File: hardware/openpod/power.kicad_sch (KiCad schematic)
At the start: 21 parts

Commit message: update power and audio
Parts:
- removed C51: 10uF, symbol Device:C
- removed LDO2: MIC5504-3.3YM5, Package_TO_SOT_SMD:SOT-23-5, symbol Regulator_Linear:MIC5504-3.3YM5
- added AP7312: ~, Package_TO_SOT_SMD:SOT-23-6, symbol openpod:AP7312
- added FB1, FB2: FerriteBead, symbol Device:FerriteBead
- C52: value 10uF -> 1uF
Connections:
- net GND: now also AP7312.2 (GND), FB2.1
- net 3.3-audio renamed +1V8
- net +1V8: now also AP7312.6 (OUT1)
- net 3.3V: no longer names the net of Buck-converter2.3 (EN), Buck-converter2.4 (FB), C50.1, L2.2
- net 3.3V: now also FB1.1
- new net +3.3V: AP7312.3 (EN2), AP7312.4 (EN1), AP7312.5 (IN), FB1.2
- new net +3.3VA: AP7312.1 (OUT2)
- new net GNDA: FB2.2

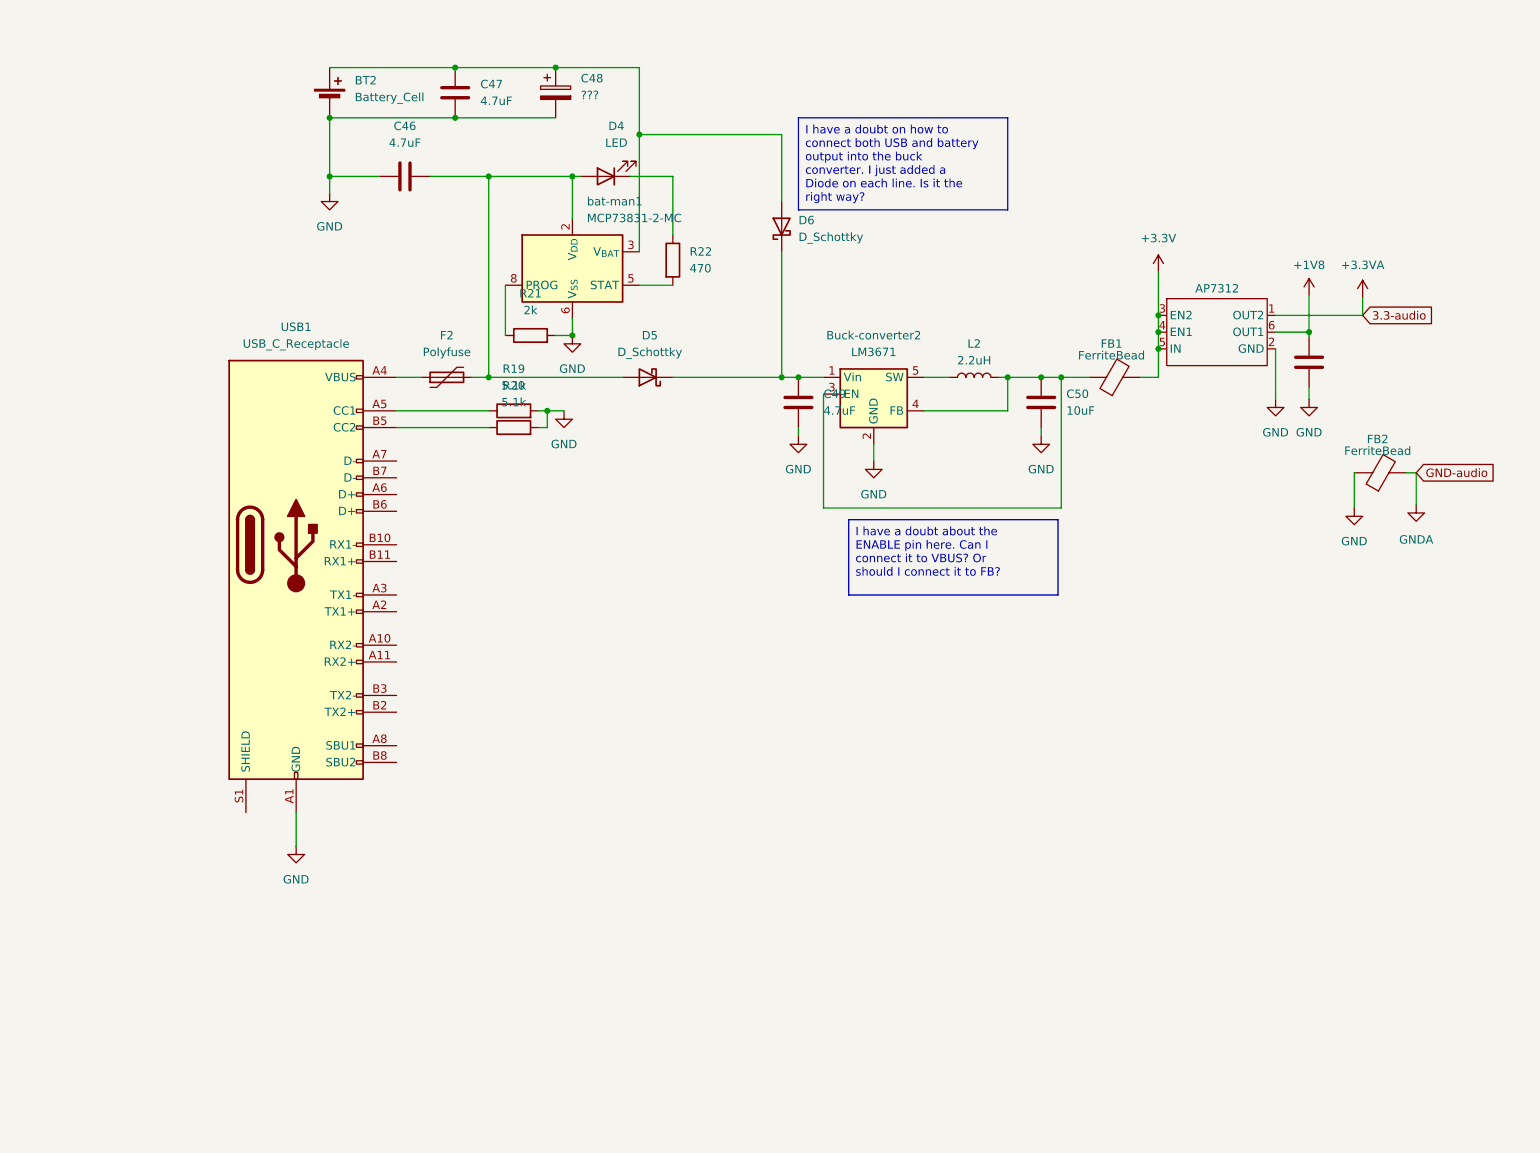
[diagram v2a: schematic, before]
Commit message: added UART converter
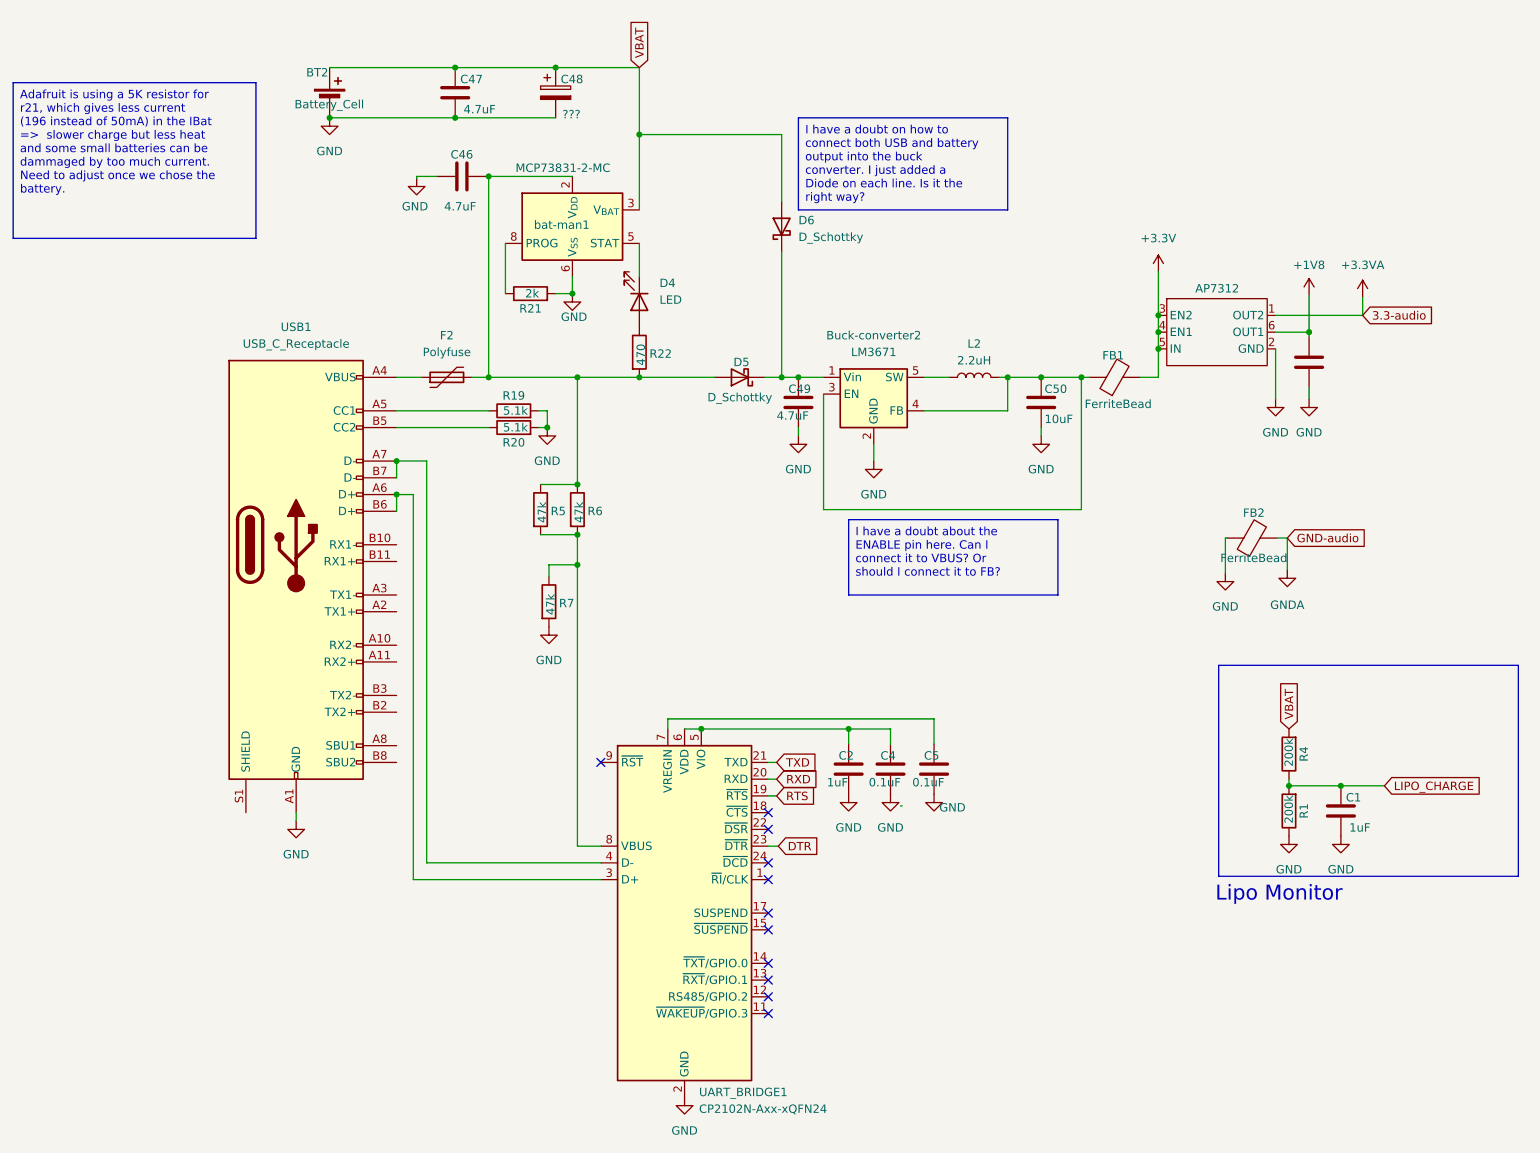
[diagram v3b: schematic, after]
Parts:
- added C1, C2: 1uF, symbol Device:C
- added C4, C5: 0.1uF, symbol Device:C
- added R1, R4: 200k, symbol Device:R
- added R5, R6, R7: 47k, symbol Device:R
- added UART_BRIDGE1: CP2102N-Axx-xQFN24, Package_DFN_QFN:QFN-24-1EP_4x4mm_P0.5mm_EP2.6x2.6mm, symbol Interface_USB:CP2102N-Axx-xQFN24
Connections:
- net GND: now also C1.2, C2.2, C4.2, C5.2, R1.1, R7.2, UART_BRIDGE1.2 (GND), UART_BRIDGE1.25 (GND)
- net at D4.1 (K): now also bat-man1.5 (STAT); no longer R22.1
- net at C46.2, D5.2 (A), F2.2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: now also R22.2, R5.1, R6.1; no longer D4.2 (A)
- net VBAT: now reaches BT2.1 (+), C47.1, C48.1, D6.2 (A), bat-man1.3 (V_{BAT}), bat-man1.4 (V_{BAT})
- net VBAT: now also R4.2
- net at USB1.A6 (D+): now also USB1.B6 (D+), UART_BRIDGE1.3 (D+)
- net at USB1.A7 (D-): now also USB1.B7 (D-), UART_BRIDGE1.4 (D-)
- new net: D4.2 (A), R22.1
- new net: C2.1, C4.1, UART_BRIDGE1.5 (VIO), UART_BRIDGE1.6 (VDD)
- new net: C5.1, UART_BRIDGE1.7 (VREGIN)
- new net: R5.2, R6.2, R7.1, UART_BRIDGE1.8 (VBUS)
- new net DTR: UART_BRIDGE1.23 (~{DTR})
- new net LIPO_CHARGE: C1.1, R1.2, R4.1
- new net RTS: UART_BRIDGE1.19 (~{RTS})
- new net RXD: UART_BRIDGE1.20 (RXD)
- new net TXD: UART_BRIDGE1.21 (TXD)
- no-connect marks 0 -> 11
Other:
- note added: "Lipo Monitor"
- moved on the sheet: C46, D4, D5, FB2, R21, R22, bat-man1

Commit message: added bluetooth
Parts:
- BT2: value Battery_Cell -> 900mah; Part number (none) -> LP053450
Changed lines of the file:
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@@
     (stroke (width 0) (type default))
   )
-  (wire (pts (xy 80.772 151.892) (xy 80.772 90.932))
+  (wire (pts (xy 95.25 151.892) (xy 95.25 90.932))
     (stroke (width 0) (type default))
   )
@@
     (stroke (width 0) (type default))
   )
-  (wire (pts (xy 78.74 154.432) (xy 107.188 154.432))
+  (wire (pts (xy 92.71 154.432) (xy 107.188 154.432))
     (stroke (width 0) (type default))
   )
@@
     (stroke (width 0) (type default))
   )
-  (wire (pts (xy 78.74 96.012) (xy 78.74 154.432))
+  (wire (pts (xy 92.71 96.012) (xy 92.71 154.432))
     (stroke (width 0) (type default))
   )
@@
     (stroke (width 0) (type default))
   )
-  (wire (pts (xy 76.2 96.012) (xy 78.74 96.012))
+  (wire (pts (xy 76.2 96.012) (xy 92.71 96.012))
     (stroke (width 0) (type default))
   )
@@
     (stroke (width 0) (type default))
   )
-  (wire (pts (xy 76.2 90.932) (xy 80.772 90.932))
-    (stroke (width 0) (type default))
-  )
-  (wire (pts (xy 107.188 151.892) (xy 80.772 151.892))
+  (wire (pts (xy 76.2 90.932) (xy 95.25 90.932))
+    (stroke (width 0) (type default))
+  )
+  (wire (pts (xy 107.188 151.892) (xy 95.25 151.892))
     (stroke (width 0) (type default))
   )
@@
       (effects (font (size 1.27 1.27)) (justify left))
     )
-    (property "Value" "Battery_Cell" (at 60.706 36.83 0)
+    (property "Value" "900mah" (at 60.706 36.83 0)
       (effects (font (size 1.27 1.27)) (justify left))
     )
@@
       (effects (font (size 1.27 1.27)) hide)
     )
-    (property "Datasheet" "~" (at 66.04 34.798 90)
-      (effects (font (size 1.27 1.27)) hide)
-    )
+    (property "Datasheet" "https://www.li-polymer-battery.com/wp-content/uploads/2021/03/LP053450_3.7V_900mAh.pdf" (at 66.04 34.798 90)
+      (effects (font (size 1.27 1.27)) hide)
+    )
+    (property "Manufacturer" "" (at 66.04 36.322 0)
+      (effects (font (size 1.27 1.27)) hide)
+    )
+    (property "Part number" "LP053450" (at 66.04 36.322 0)
+      (effects (font (size 1.27 1.27)) hide)
+    )
+    (property "Supplier" "" (at 66.04 36.322 0)
+      (effects (font (size 1.27 1.27)) hide)
+    )
+    (property "Supplier Part number" "" (at 66.04 36.322 0)
+      (effects (font (size 1.27 1.27)) hide)
+    )
